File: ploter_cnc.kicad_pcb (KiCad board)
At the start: 2 copper layers, 49 x 26 mm, 7 parts, among them J1 Conn_01x05_Socket, J2 Conn_01x05_Socket, J3 Conn_01x05_Socket, J4 Conn_01x02_Socket, U1 ULN2803A, U2 ULN2803A

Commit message: primera version a imprimir
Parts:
- added C1: 100 nf, Capacitor_THT:C_Disc_D4.3mm_W1.9mm_P5.00mm, F.Cu at (143.5, 119.2)
- added C2: 100 µF, Capacitor_THT:CP_Radial_D4.0mm_P2.00mm, F.Cu at (140.5, 132.5)
- added H1: MountingHole, MountingHole:MountingHole_2.2mm_M2_DIN965_Pad, F.Cu at (177.5, 62.8)
- added H2: MountingHole, MountingHole:MountingHole_2.2mm_M2_DIN965_Pad, F.Cu at (127.5, 62.8)
- added H3: MountingHole, MountingHole:MountingHole_2.2mm_M2_DIN965_Pad, F.Cu at (127.5, 141.8)
- added H4: MountingHole, MountingHole:MountingHole_2.2mm_M2_DIN965_Pad, F.Cu at (177.5, 141.8)
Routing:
- net GND: track 90.9 -> 98.0 mm
- net VCC: track 168.7 -> 174.1 mm
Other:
- board size 49 x 26 mm -> 60 x 90 mm

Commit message: cableado correjido, y relleno
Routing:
- net Net-(U2-O1): track 0.00 -> 61.5 mm
- net GND: track 98.0 -> 112.6 mm
- net Net-(U2-O7): track 0.00 -> 12.1 mm
- net Net-(U2-O8): track 0.00 -> 12.1 mm
- net Net-(U2-O3): track 0.00 -> 11.0 mm
- net Net-(U2-O2): track 0.00 -> 11.0 mm
- net Net-(U2-O6): track 0.00 -> 10.0 mm
- net Net-(U2-O5): track 0.00 -> 10.0 mm
- net Net-(U2-O4): track 0.00 -> 10.0 mm
- added copper zone on B.Cu, net GND
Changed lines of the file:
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@@
 	)
 	(segment
-		(start 138.3284 125.349)
-		(end 138.4046 125.4252)
+		(start 138.4046 119.3454)
+		(end 138.5 119.25)
+		(width 1.5)
+		(layer "B.Cu")
+		(net "GND")
+	)
+	(segment
+		(start 124.968 99.0346)
+		(end 124.968 116.8146)
 		(width 1.5)
 		(layer "B.Cu")
@@
 	)
 	(segment
+		(start 138.4046 125.4252)
+		(end 138.4046 119.3454)
+		(width 1.5)
+		(layer "B.Cu")
+		(net "GND")
+	)
+	(segment
 		(start 136.652 70.2056)
 		(end 132.0546 70.2056)
@@
 	)
 	(segment
-		(start 138.3284 99.0346)
-		(end 138.3284 125.349)
+		(start 124.968 116.8146)
+		(end 133.5786 125.4252)
+		(width 1.5)
+		(layer "B.Cu")
+		(net "GND")
+	)
+	(segment
+		(start 133.5786 125.4252)
+		(end 138.4046 125.4252)
 		(width 1.5)
 		(layer "B.Cu")
@@
 	)
 	(segment
+		(start 171.3484 112.395)
+		(end 171.3484 114.6048)
+		(width 1.5)
+		(layer "B.Cu")
+		(net "Net-(U2-O8)")
+	)
+	(segment
+		(start 166.1414 119.8118)
+		(end 166.1414 122.3518)
+		(width 1.5)
+		(layer "B.Cu")
+		(net "Net-(U2-O8)")
+	)
+	(segment
+		(start 171.3484 114.6048)
+		(end 166.1414 119.8118)
+		(width 1.5)
+		(layer "B.Cu")
+		(net "Net-(U2-O8)")
+	)
+	(segment
+		(start 163.6014 119.1514)
+		(end 168.8084 113.9444)
+		(width 1.5)
+		(layer "B.Cu")
+		(net "Net-(U2-O7)")
+	)
+	(segment
+		(start 163.6014 122.3518)
+		(end 163.6014 119.1514)
+		(width 1.5)
+		(layer "B.Cu")
+		(net "Net-(U2-O7)")
+	)
+	(segment
+		(start 168.8084 113.9444)
+		(end 168.8084 112.395)
+		(width 1.5)
+		(layer "B.Cu")
+		(net "Net-(U2-O7)")
+	)
+	(segment
+		(start 161.1884 112.395)
+		(end 161.1884 122.2248)
+		(width 1.5)
+		(layer "B.Cu")
+		(net "Net-(U2-O6)")
+	)
+	(segment
+		(start 161.1884 122.2248)
+		(end 161.0614 122.3518)
+		(width 1.5)
+		(layer "B.Cu")
+		(net "Net-(U2-O6)")
+	)
+	(segment
+		(start 158.5214 112.522)
+		(end 158.6484 112.395)
+		(width 1.5)
+		(layer "B.Cu")
+		(net "Net-(U2-O5)")
+	)
+	(segment
+		(start 158.5214 122.3518)
+		(end 158.5214 112.522)
+		(width 1.5)
+		(layer "B.Cu")
+		(net "Net-(U2-O5)")
+	)
+	(segment
+		(start 156.1084 122.2248)
+		(end 155.9814 122.3518)
+		(width 1.5)
+		(layer "B.Cu")
+		(net "Net-(U2-O4)")
+	)
+	(segment
+		(start 156.1084 112.395)
+		(end 156.1084 122.2248)
+		(width 1.5)
+		(layer "B.Cu")
+		(net "Net-(U2-O4)")
+	)
+	(segment
+		(start 153.4414 115.443)
+		(end 153.4414 122.3518)
+		(width 1.5)
+		(layer "B.Cu")
+		(net "Net-(U2-O3)")
+	)
+	(segment
+		(start 151.0284 113.03)
+		(end 153.4414 115.443)
+		(width 1.5)
+		(layer "B.Cu")
+		(net "Net-(U2-O3)")
+	)
+	(segment
+		(start 151.0284 112.395)
+		(end 151.0284 113.03)
+		(width 1.5)
+		(layer "B.Cu")
+		(net "Net-(U2-O3)")
+	)
+	(segment
+		(start 148.4884 113.4618)
+		(end 148.4884 112.395)
+		(width 1.5)
+		(layer "B.Cu")
+		(net "Net-(U2-O2)")
+	)
+	(segment
+		(start 150.9014 115.8748)
+		(end 148.4884 113.4618)
+		(width 1.5)
+		(layer "B.Cu")
+		(net "Net-(U2-O2)")
+	)
+	(segment
+		(start 150.9014 122.3518)
+		(end 150.9014 115.8748)
+		(width 1.5)
+		(layer "B.Cu")
+		(net "Net-(U2-O2)")
+	)
+	(segment
+		(start 137.7442 106.0704)
+		(end 140.8684 102.9462)
+		(width 1.5)
+		(layer "B.Cu")
+		(net "Net-(U2-O1)")
+	)
+	(segment
+		(start 148.3614 122.3518)
+		(end 148.3614 120.4518)
+		(width 1.5)
+		(layer "B.Cu")
+		(net "Net-(U2-O1)")
+	)
+	(segment
+		(start 129.5654 115.8494)
+		(end 127.918213 114.202213)
+		(width 1.5)
+		(layer "B.Cu")
+		(net "Net-(U2-O1)")
+	)
+	(segment
+		(start 130.9624 106.0704)
+		(end 137.7442 106.0704)
+		(width 1.5)
+		(layer "B.Cu")
+		(net "Net-(U2-O1)")
+	)
+	(segment
+		(start 127.918213 114.202213)
+		(end 127.918213 109.114587)
+		(width 1.5)
+		(layer "B.Cu")
+		(net "Net-(U2-O1)")
+	)
+	(segment
+		(start 140.8684 102.9462)
+		(end 140.8684 86.995)
+		(width 1.5)
+		(layer "B.Cu")
+		(net "Net-(U2-O1)")
+	)
+	(segment
+		(start 143.759 115.8494)
+		(end 129.5654 115.8494)
+		(width 1.5)
+		(layer "B.Cu")
+		(net "Net-(U2-O1)")
+	)
+	(segment
+		(start 127.918213 109.114587)
+		(end 130.9624 106.0704)
+		(width 1.5)
+		(layer "B.Cu")
+		(net "Net-(U2-O1)")
+	)
+	(segment
+		(start 148.3614 120.4518)
+		(end 143.759 115.8494)
+		(width 1.5)
+		(layer "B.Cu")
+		(net "Net-(U2-O1)")
+	)
+	(segment
 		(start 145.9484 83.6676)
 		(end 149.352 80.264)
@@
 		(net "Net-(U1-O1)")
 	)
+	(zone
+		(net "GND")
+		(layer "B.Cu")
+		(hatch edge 0.5)
+		(connect_pads
+			(clearance 0.5)
+		)
+		(min_thickness 0.25)
+		(fill yes
+			(thermal_gap 0.5)
+			(thermal_bridge_width 0.5)
+			(island_removal_mode 0)
+		)
+		(polygon
+			(pts
+				(xy 122.2502 147.8788) (xy 183.515 147.6248) (xy 183.515 55.6006) (xy 121.4882 55.6006) (xy 122.252319 147.880727)
+				(xy 122.255632 147.883739)
+			)
+		)
+	)
 	(embedded_fonts no)

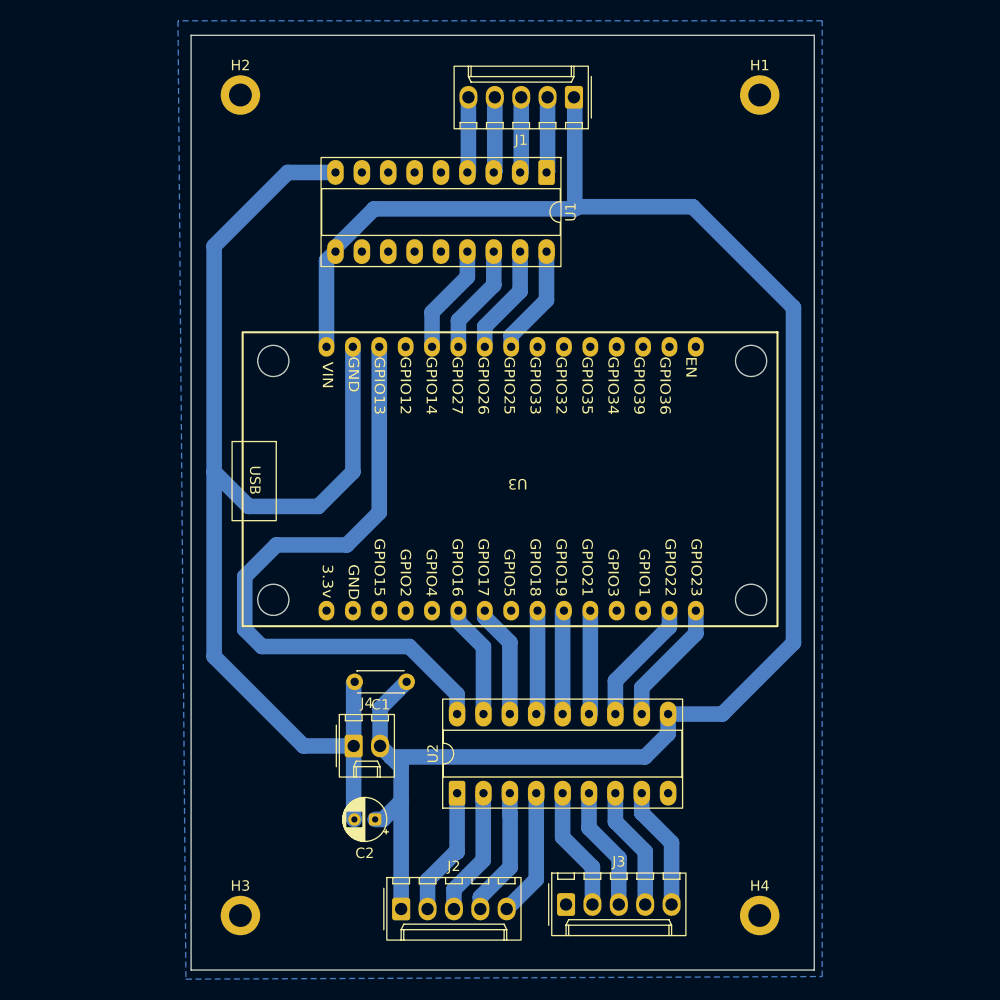
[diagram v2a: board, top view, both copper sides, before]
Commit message: fix rutas e inversion final del circuito
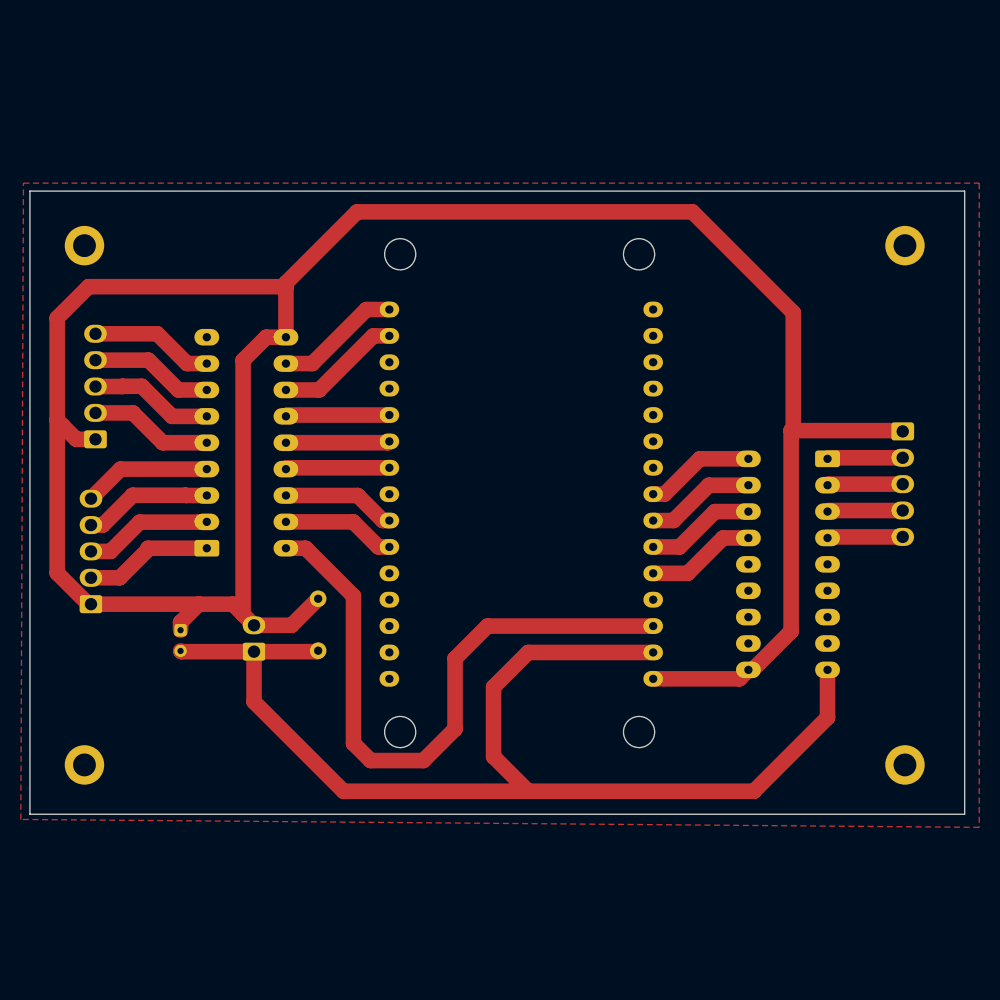
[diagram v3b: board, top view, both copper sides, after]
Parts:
- C1, C2, H1, H2, H3, H4, J1, J2, J3, J4, U1, U2, U3: moved to B.Cu
- moved H4 91.6 mm to (112.5, 77.2), turned to 90 degrees
- moved H2 90.9 mm to (191.5, 127.2), turned to 90 degrees
- moved J3 63.7 mm to (113.5, 95.9), turned to 90 degrees
- moved J1 45.1 mm to (191.3, 95.1), turned to -90 degrees
- moved J2 41.9 mm to (113.1, 111.8), turned to 90 degrees
- moved U1 38.6 mm to (184.0, 97.8), turned to 180 degrees
- moved U2 33.7 mm to (124.3, 106.4), turned to 0 degrees
- moved C2 26.1 mm to (121.7, 114.3), turned to -90 degrees
- moved H3 20.9 mm to (112.5, 127.2), turned to 90 degrees
- moved H1 20.1 mm to (191.5, 77.2), turned to 90 degrees
- moved J4 13.2 mm to (128.8, 116.3), turned to 90 degrees
- moved C1 11.7 mm to (135.0, 111.2), turned to -90 degrees
- moved U3 3.92 mm to (155.3, 101.9), turned to 180 degrees
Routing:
- net VCC: track 174.1 -> 230.9 mm
- added copper zone on F.Cu, net GND
- removed copper zone on B.Cu, net GND
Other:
- board size 60 x 90 mm -> 90 x 60 mm

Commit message: xlas
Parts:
- J2, J3: moved to F.Cu
- moved U2 23.9 mm to (132.8, 84.1), turned to 180 degrees
- moved J1 16.5 mm to (187.8, 111.3), turned to 90 degrees
- moved J2 16.0 mm to (115.8, 96.0), turned to -90 degrees
- moved J3 15.6 mm to (119.4, 81.5), turned to -90 degrees
- moved U1 15.5 mm to (173.2, 108.8), turned to 0 degrees
- moved C1 7.89 mm to (136.3, 119.0), turned to 90 degrees
- moved H2 4.70 mm to (187.9, 124.2)
- moved H3 4.16 mm to (115.0, 123.9)
- moved H1 3.40 mm to (188.1, 77.3)
- moved H4 2.53 mm to (115.0, 76.8)
- moved J4 2.13 mm to (129.2, 114.2), turned to -90 degrees
- moved C2 2.00 mm to (121.8, 116.3), turned to 90 degrees
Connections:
- J2 pad 2: A1 -> Net-(J2-Pin_2)
- J2 pad 3: B1 -> Net-(J2-Pin_3)
- J2 pad 4: C1 -> Net-(J2-Pin_4)
- J2 pad 5: D1 -> Net-(J2-Pin_5)
- J3 pad 2: A2 -> D2
- J3 pad 3: B2 -> C2
- J3 pad 4: C2 -> B2
- J3 pad 5: D2 -> A2
- U1 pad 1: A -> Net-(U1-I1)
- U1 pad 15: Net-(U1-O4) -> D
- U1 pad 16: Net-(U1-O3) -> C
- U1 pad 17: Net-(U1-O2) -> B
- U1 pad 18: Net-(U1-O1) -> A
- U1 pad 2: B -> Net-(U1-I2)
- U1 pad 3: C -> Net-(U1-I3)
- U1 pad 4: D -> Net-(U1-I4)
- U2 pad 1: A1 -> Net-(U2-I1)
- U2 pad 11: Net-(U2-O8) -> Net-(J2-Pin_5)
- U2 pad 12: Net-(U2-O7) -> Net-(J2-Pin_4)
- U2 pad 13: Net-(U2-O6) -> Net-(J2-Pin_3)
- U2 pad 14: Net-(U2-O5) -> Net-(J2-Pin_2)
- U2 pad 15: Net-(U2-O4) -> A2
- U2 pad 16: Net-(U2-O3) -> B2
- U2 pad 17: Net-(U2-O2) -> C2
- U2 pad 18: Net-(U2-O1) -> D2
- U2 pad 2: B1 -> Net-(U2-I2)
- U2 pad 3: C1 -> Net-(U2-I3)
- U2 pad 4: D1 -> Net-(U2-I4)
- U2 pad 5: A2 -> Net-(U2-I5)
- U2 pad 6: B2 -> Net-(U2-I6)
- U2 pad 7: C2 -> Net-(U2-I7)
- U2 pad 8: D2 -> Net-(U2-I8)
- U3 pad 21: Net-(U2-O2) -> Net-(U2-I7)
- U3 pad 22: Net-(U2-O3) -> Net-(U2-I6)
- U3 pad 24: Net-(U2-O4) -> Net-(U2-I5)
- U3 pad 25: Net-(U2-O5) -> Net-(U2-I4)
- U3 pad 26: Net-(U2-O6) -> Net-(U2-I3)
- U3 pad 29: Net-(U2-O7) -> Net-(U2-I2)
- U3 pad 3: Net-(U2-O1) -> Net-(U2-I8)
- U3 pad 30: Net-(U2-O8) -> Net-(U2-I1)
- U3 pad 5: Net-(U1-O4) -> Net-(U1-I1)
- U3 pad 6: Net-(U1-O3) -> Net-(U1-I2)
- U3 pad 7: Net-(U1-O2) -> Net-(U1-I3)
- U3 pad 8: Net-(U1-O1) -> Net-(U1-I4)
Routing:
- net Net-(U2-I8): track 0.00 -> 82.7 mm
- net VCC: track 230.9 -> 164.5 mm
- net Net-(U2-O1): track 61.5 -> 0.00 mm
- net GND: track 112.6 -> 68.7 mm
- net A1: track 12.4 -> 0.00 mm
- net C1: track 12.3 -> 0.00 mm
- net B1: track 12.3 -> 0.00 mm
- net D1: track 12.3 -> 0.00 mm
- net Net-(U2-O7): track 12.1 -> 0.00 mm
- net Net-(U2-O8): track 12.1 -> 0.00 mm
- net Net-(U2-I7): track 0.00 -> 11.9 mm
- net Net-(U2-I6): track 0.00 -> 11.9 mm
- net Net-(U2-I3): track 0.00 -> 11.5 mm
- net Net-(J2-Pin_5): track 0.00 -> 11.2 mm
- net Net-(J2-Pin_4): track 0.00 -> 11.2 mm
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- removed copper zone on F.Cu, net GND
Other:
- board size 90 x 60 mm -> 86.5 x 54.9 mm
